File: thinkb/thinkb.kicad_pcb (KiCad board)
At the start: 2 copper layers, 2 parts, among them SW1 SW_Push

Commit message: Working on the PCB
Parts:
- added D10: 1N4148, footprints:diode_TH_SMD, F.Cu at (217.2, 48.7)
- added D11: 1N4148, footprints:diode_TH_SMD, F.Cu at (235.8, 48.9)
- added D12: 1N4148, footprints:diode_TH_SMD, F.Cu at (253.9, 49.6)
- added D13: 1N4148, footprints:diode_TH_SMD, F.Cu at (50.9, 65.8)
- added D14: 1N4148, footprints:diode_TH_SMD, F.Cu at (69.5, 65.7)
- added D15: 1N4148, footprints:diode_TH_SMD, F.Cu at (88.3, 66.0)
- added D16: 1N4148, footprints:diode_TH_SMD, F.Cu at (106.3, 66.1)
- added D17: 1N4148, footprints:diode_TH_SMD, F.Cu at (125.3, 67.1)
- added D18: 1N4148, footprints:diode_TH_SMD, F.Cu at (142.9, 66.8)
- added D19: 1N4148, footprints:diode_TH_SMD, F.Cu at (162.5, 66.8)
- added D2: 1N4148, footprints:diode_TH_SMD, F.Cu at (69.5, 48.2)
- added D20: 1N4148, footprints:diode_TH_SMD, F.Cu at (179.5, 66.0)
- added D21: 1N4148, footprints:diode_TH_SMD, F.Cu at (197.6, 66.0)
- added D22: 1N4148, footprints:diode_TH_SMD, F.Cu at (216.5, 65.8)
- added D23: 1N4148, footprints:diode_TH_SMD, F.Cu at (235.2, 66.1)
- added D24: 1N4148, footprints:diode_TH_SMD, F.Cu at (253.0, 65.8)
- added D25: 1N4148, footprints:diode_TH_SMD, F.Cu at (51.4, 83.1)
- added D26: 1N4148, footprints:diode_TH_SMD, F.Cu at (69.9, 82.4)
- added D27: 1N4148, footprints:diode_TH_SMD, F.Cu at (87.3, 82.7)
- added D28: 1N4148, footprints:diode_TH_SMD, F.Cu at (106.3, 82.8)
- added D29: 1N4148, footprints:diode_TH_SMD, F.Cu at (125.4, 83.0)
- added D3: 1N4148, footprints:diode_TH_SMD, F.Cu at (87.5, 47.9)
- added D30: 1N4148, footprints:diode_TH_SMD, F.Cu at (144.0, 82.8)
- added D31: 1N4148, footprints:diode_TH_SMD, F.Cu at (162.0, 82.9)
- added D32: 1N4148, footprints:diode_TH_SMD, F.Cu at (180.3, 83.1)
- added D33: 1N4148, footprints:diode_TH_SMD, F.Cu at (198.2, 83.4)
- added D34: 1N4148, footprints:diode_TH_SMD, F.Cu at (217.2, 83.0)
- added D35: 1N4148, footprints:diode_TH_SMD, F.Cu at (235.2, 82.8)
- added D36: 1N4148, footprints:diode_TH_SMD, F.Cu at (253.0, 82.9)
- added D37: 1N4148, footprints:diode_TH_SMD, F.Cu at (51.3, 100.7)
- added D38: 1N4148, footprints:diode_TH_SMD, F.Cu at (71.1, 98.1)
- added D39: 1N4148, footprints:diode_TH_SMD, F.Cu at (89.5, 99.1)
- added D4: 1N4148, footprints:diode_TH_SMD, F.Cu at (105.7, 48.9)
- added D40: 1N4148, footprints:diode_TH_SMD, F.Cu at (106.4, 99.7)
- added D41: 1N4148, footprints:diode_TH_SMD, F.Cu at (125.6, 100.1)
- added D42: 1N4148, footprints:diode_TH_SMD, F.Cu at (143.7, 100.2)
- added D43: 1N4148, footprints:diode_TH_SMD, F.Cu at (162.6, 99.4)
- added D44: 1N4148, footprints:diode_TH_SMD, F.Cu at (180.5, 99.5)
- added D45: 1N4148, footprints:diode_TH_SMD, F.Cu at (198.6, 100.3)
- added D46: 1N4148, footprints:diode_TH_SMD, F.Cu at (216.8, 99.9)
- added D47: 1N4148, footprints:diode_TH_SMD, F.Cu at (234.9, 99.9)
- added D48: 1N4148, footprints:diode_TH_SMD, F.Cu at (253.6, 100.5)
- added D49: 1N4148, footprints:diode_TH_SMD, F.Cu at (51.3, 116.4)
- added D5: 1N4148, footprints:diode_TH_SMD, F.Cu at (124.5, 49.9)
- added D50: 1N4148, footprints:diode_TH_SMD, F.Cu at (69.9, 116.3)
- added D51: 1N4148, footprints:diode_TH_SMD, F.Cu at (88.9, 115.9)
- added D52: 1N4148, footprints:diode_TH_SMD, F.Cu at (107.8, 116.8)
- added D53: 1N4148, footprints:diode_TH_SMD, F.Cu at (126.4, 117.2)
- added D54: 1N4148, footprints:diode_TH_SMD, F.Cu at (144.1, 116.3)
- added D55: 1N4148, footprints:diode_TH_SMD, F.Cu at (161.7, 116.6)
- added D56: 1N4148, footprints:diode_TH_SMD, F.Cu at (180.5, 116.0)
- added D57: 1N4148, footprints:diode_TH_SMD, F.Cu at (198.7, 116.4)
- added D58: 1N4148, footprints:diode_TH_SMD, F.Cu at (216.5, 116.8)
- added D59: 1N4148, footprints:diode_TH_SMD, F.Cu at (234.1, 116.8)
- added D6: 1N4148, footprints:diode_TH_SMD, F.Cu at (143.8, 49.1)
- added D60: 1N4148, footprints:diode_TH_SMD, F.Cu at (253.3, 116.9)
- added D7: 1N4148, footprints:diode_TH_SMD, F.Cu at (162.6, 49.0)
- added D8: 1N4148, footprints:diode_TH_SMD, F.Cu at (180.2, 48.5)
- added D9: 1N4148, footprints:diode_TH_SMD, F.Cu at (198.6, 48.4)
- added SW10: SW_Push, footprints:Choc_PG1350_Choc_Spacing, F.Cu at (215.6, 45.2)
- added SW11: SW_Push, footprints:Choc_PG1350_Choc_Spacing, F.Cu at (234.0, 45.6)
- added SW12: SW_Push, footprints:Choc_PG1350_Choc_Spacing, F.Cu at (252.0, 45.9)
- added SW13: SW_Push, footprints:Choc_PG1350_Choc_Spacing, F.Cu at (49.4, 62.4)
- added SW14: SW_Push, footprints:Choc_PG1350_Choc_Spacing, F.Cu at (67.9, 62.3)
- added SW15: SW_Push, footprints:Choc_PG1350_Choc_Spacing, F.Cu at (86.3, 62.4)
- added SW16: SW_Push, footprints:Choc_PG1350_Choc_Spacing, F.Cu at (104.3, 62.6)
- added SW17: SW_Push, footprints:Choc_PG1350_Choc_Spacing, F.Cu at (123.0, 63.1)
- added SW18: SW_Push, footprints:Choc_PG1350_Choc_Spacing, F.Cu at (141.5, 63.2)
- added SW19: SW_Push, footprints:Choc_PG1350_Choc_Spacing, F.Cu at (160.2, 63.2)
- added SW2: SW_Push, footprints:Choc_PG1350_Choc_Spacing, F.Cu at (67.4, 44.8)
- added SW20: SW_Push, footprints:Choc_PG1350_Choc_Spacing, F.Cu at (178.3, 62.5)
- added SW21: SW_Push, footprints:Choc_PG1350_Choc_Spacing, F.Cu at (196.5, 62.5)
- added SW22: SW_Push, footprints:Choc_PG1350_Choc_Spacing, F.Cu at (214.9, 62.4)
- added SW23: SW_Push, footprints:Choc_PG1350_Choc_Spacing, F.Cu at (233.4, 62.5)
- added SW24: SW_Push, footprints:Choc_PG1350_Choc_Spacing, F.Cu at (251.6, 62.6)
- added SW25: SW_Push, footprints:Choc_PG1350_Choc_Spacing, F.Cu at (49.2, 79.5)
- added SW26: SW_Push, footprints:Choc_PG1350_Choc_Spacing, F.Cu at (67.8, 79.1)
- added SW27: SW_Push, footprints:Choc_PG1350_Choc_Spacing, F.Cu at (86.3, 79.2)
- added SW28: SW_Push, footprints:Choc_PG1350_Choc_Spacing, F.Cu at (104.4, 79.1)
- added SW29: SW_Push, footprints:Choc_PG1350_Choc_Spacing, F.Cu at (123.7, 79.3)
- added SW3: SW_Push, footprints:Choc_PG1350_Choc_Spacing, F.Cu at (85.6, 44.4)
- added SW30: SW_Push, footprints:Choc_PG1350_Choc_Spacing, F.Cu at (142.1, 79.3)
- added SW31: SW_Push, footprints:Choc_PG1350_Choc_Spacing, F.Cu at (160.3, 79.6)
- added SW32: SW_Push, footprints:Choc_PG1350_Choc_Spacing, F.Cu at (178.4, 79.5)
- added SW33: SW_Push, footprints:Choc_PG1350_Choc_Spacing, F.Cu at (196.5, 79.9)
- added SW34: SW_Push, footprints:Choc_PG1350_Choc_Spacing, F.Cu at (214.7, 79.5)
- added SW35: SW_Push, footprints:Choc_PG1350_Choc_Spacing, F.Cu at (233.1, 79.4)
- added SW36: SW_Push, footprints:Choc_PG1350_Choc_Spacing, F.Cu at (251.9, 79.7)
- added SW37: SW_Push, footprints:Choc_PG1350_Choc_Spacing, F.Cu at (49.5, 96.9)
- added SW38: SW_Push, footprints:Choc_PG1350_Choc_Spacing, F.Cu at (69.4, 94.8)
- added SW39: SW_Push, footprints:Choc_PG1350_Choc_Spacing, F.Cu at (87.7, 95.7)
- added SW4: SW_Push, footprints:Choc_PG1350_Choc_Spacing, F.Cu at (104.1, 45.4)
- added SW40: SW_Push, footprints:Choc_PG1350_Choc_Spacing, F.Cu at (104.7, 96.1)
- added SW41: SW_Push, footprints:Choc_PG1350_Choc_Spacing, F.Cu at (123.7, 96.7)
- added SW42: SW_Push, footprints:Choc_PG1350_Choc_Spacing, F.Cu at (141.9, 96.5)
- added SW43: SW_Push, footprints:Choc_PG1350_Choc_Spacing, F.Cu at (160.4, 96.2)
- added SW44: SW_Push, footprints:Choc_PG1350_Choc_Spacing, F.Cu at (178.8, 96.2)
- added SW45: SW_Push, footprints:Choc_PG1350_Choc_Spacing, F.Cu at (196.5, 96.8)
- added SW46: SW_Push, footprints:Choc_PG1350_Choc_Spacing, F.Cu at (214.7, 96.5)
- added SW47: SW_Push, footprints:Choc_PG1350_Choc_Spacing, F.Cu at (232.9, 96.2)
- added SW48: SW_Push, footprints:Choc_PG1350_Choc_Spacing, F.Cu at (251.4, 97.0)
- added SW49: SW_Push, footprints:Choc_PG1350_Choc_Spacing, F.Cu at (49.3, 112.9)
- added SW5: SW_Push, footprints:Choc_PG1350_Choc_Spacing, F.Cu at (122.7, 46.3)
- added SW50: SW_Push, footprints:Choc_PG1350_Choc_Spacing, F.Cu at (68.4, 112.9)
- added SW51: SW_Push, footprints:Choc_PG1350_Choc_Spacing, F.Cu at (87.1, 112.7)
- added SW52: SW_Push, footprints:Choc_PG1350_Choc_Spacing, F.Cu at (106.6, 113.3)
- added SW53: SW_Push, footprints:Choc_PG1350_Choc_Spacing, F.Cu at (124.5, 113.3)
- added SW54: SW_Push, footprints:Choc_PG1350_Choc_Spacing, F.Cu at (142.1, 113.0)
- added SW55: SW_Push, footprints:Choc_PG1350_Choc_Spacing, F.Cu at (160.2, 113.1)
- added SW56: SW_Push, footprints:Choc_PG1350_Choc_Spacing, F.Cu at (178.7, 112.6)
- added SW57: SW_Push, footprints:Choc_PG1350_Choc_Spacing, F.Cu at (196.8, 113.0)
- added SW58: SW_Push, footprints:Choc_PG1350_Choc_Spacing, F.Cu at (215.0, 113.2)
- added SW59: SW_Push, footprints:Choc_PG1350_Choc_Spacing, F.Cu at (232.4, 113.3)
- added SW6: SW_Push, footprints:Choc_PG1350_Choc_Spacing, F.Cu at (141.4, 45.5)
- added SW60: SW_Push, footprints:Choc_PG1350_Choc_Spacing, F.Cu at (251.3, 113.2)
- added SW7: SW_Push, footprints:Choc_PG1350_Choc_Spacing, F.Cu at (160.6, 45.5)
- added SW8: SW_Push, footprints:Choc_PG1350_Choc_Spacing, F.Cu at (178.4, 45.2)
- added SW9: SW_Push, footprints:Choc_PG1350_Choc_Spacing, F.Cu at (196.7, 45.0)
- D1: footprint Diode_THT:D_DO-35_SOD27_P7.62mm_Horizontal -> footprints:diode_TH_SMD
- moved SW1 101.3 mm to (49.4, 44.8)
- moved D1 94.0 mm to (51.1, 48.3), turned to 0 degrees

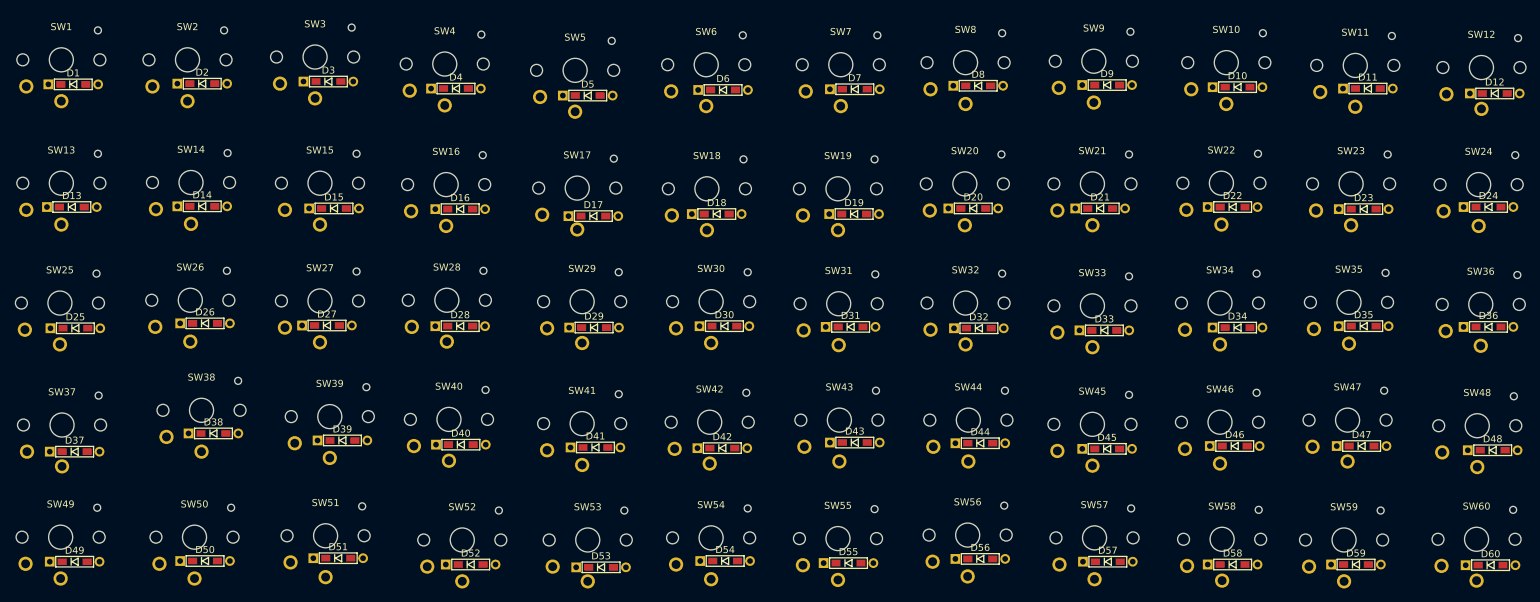
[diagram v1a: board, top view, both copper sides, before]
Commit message: Aligned all the switches
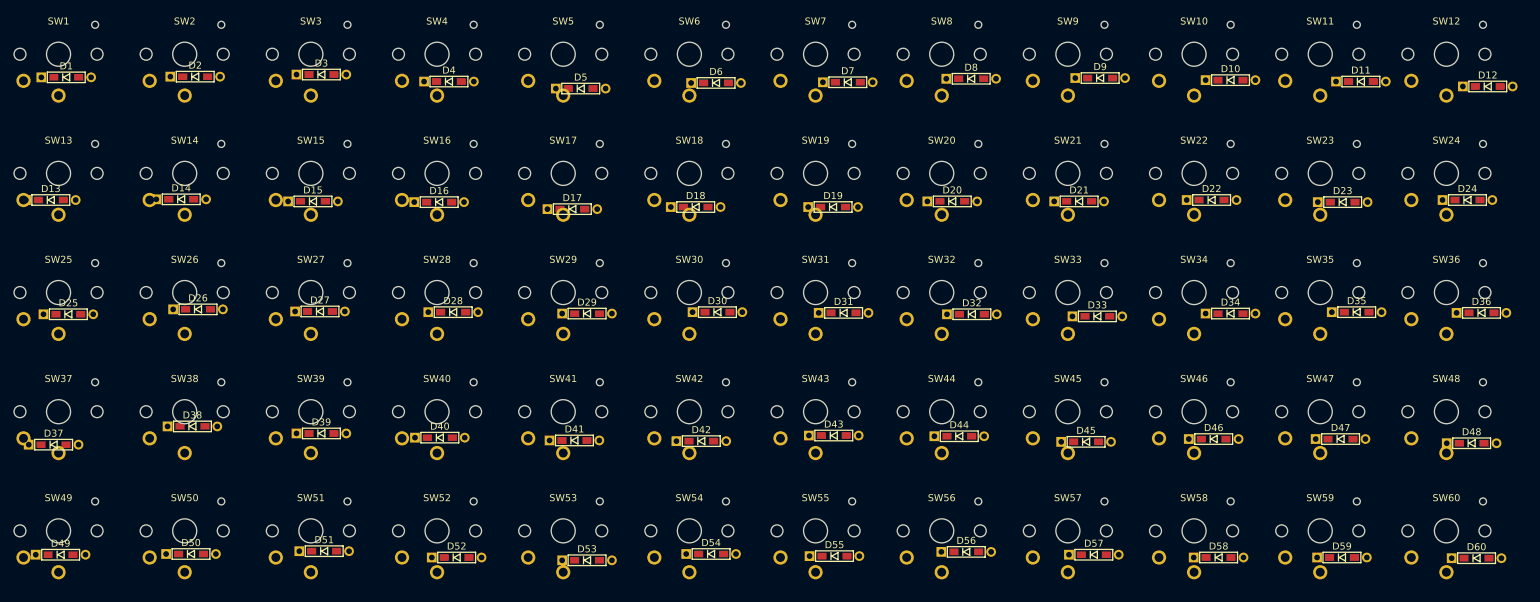
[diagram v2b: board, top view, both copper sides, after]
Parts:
- moved SW12 5.35 mm to (247.0, 44.0)
- moved SW11 5.25 mm to (229.0, 44.0)
- moved SW36 5.19 mm to (247.0, 78.0)
- moved SW24 4.87 mm to (247.0, 61.0)
- moved SW48 4.83 mm to (247.0, 95.0)
- moved SW10 4.75 mm to (211.0, 44.0)
- moved SW23 4.65 mm to (229.0, 61.0)
- moved SW60 4.46 mm to (247.0, 112.0)
- moved SW35 4.33 mm to (229.0, 78.0)
- moved SW58 4.18 mm to (211.0, 112.0)
- moved SW22 4.14 mm to (211.0, 61.0)
- moved SW47 4.08 mm to (229.0, 95.0)
- moved SW34 3.99 mm to (211.0, 78.0)
- moved SW46 3.99 mm to (211.0, 95.0)
- moved SW44 3.98 mm to (175.0, 95.0)
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
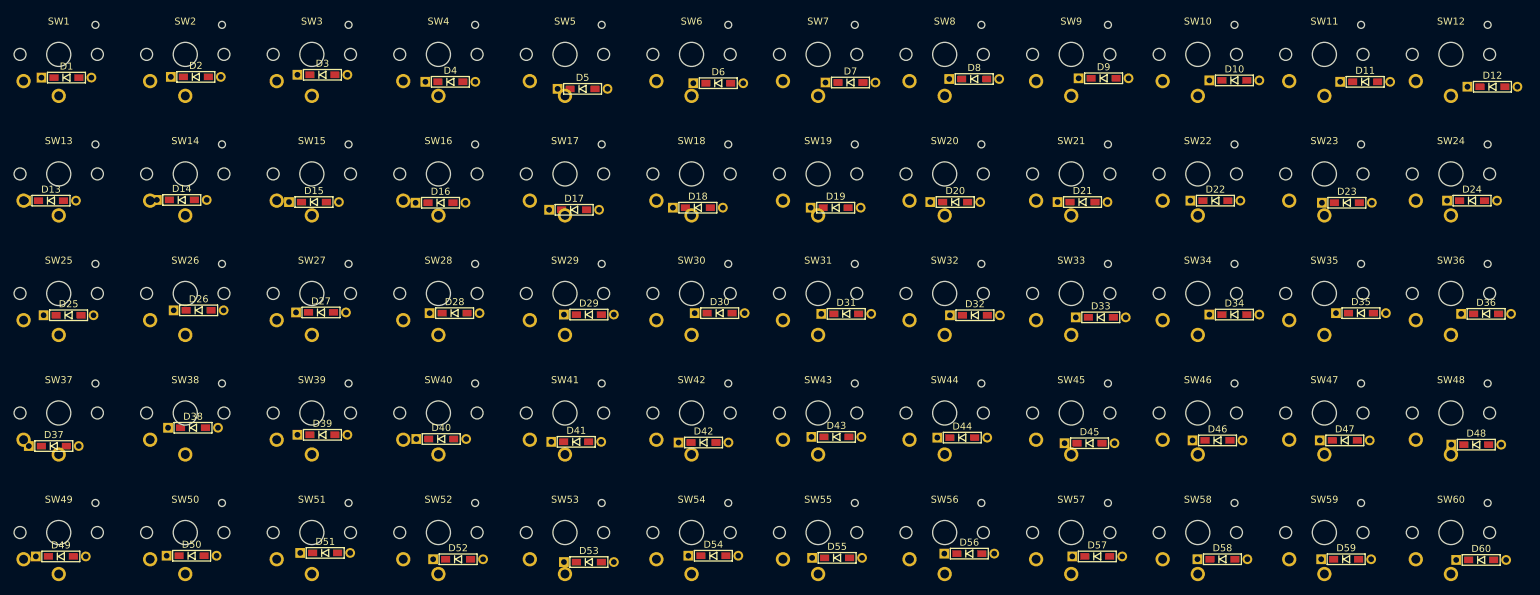
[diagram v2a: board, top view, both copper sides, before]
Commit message: Aligned diodes
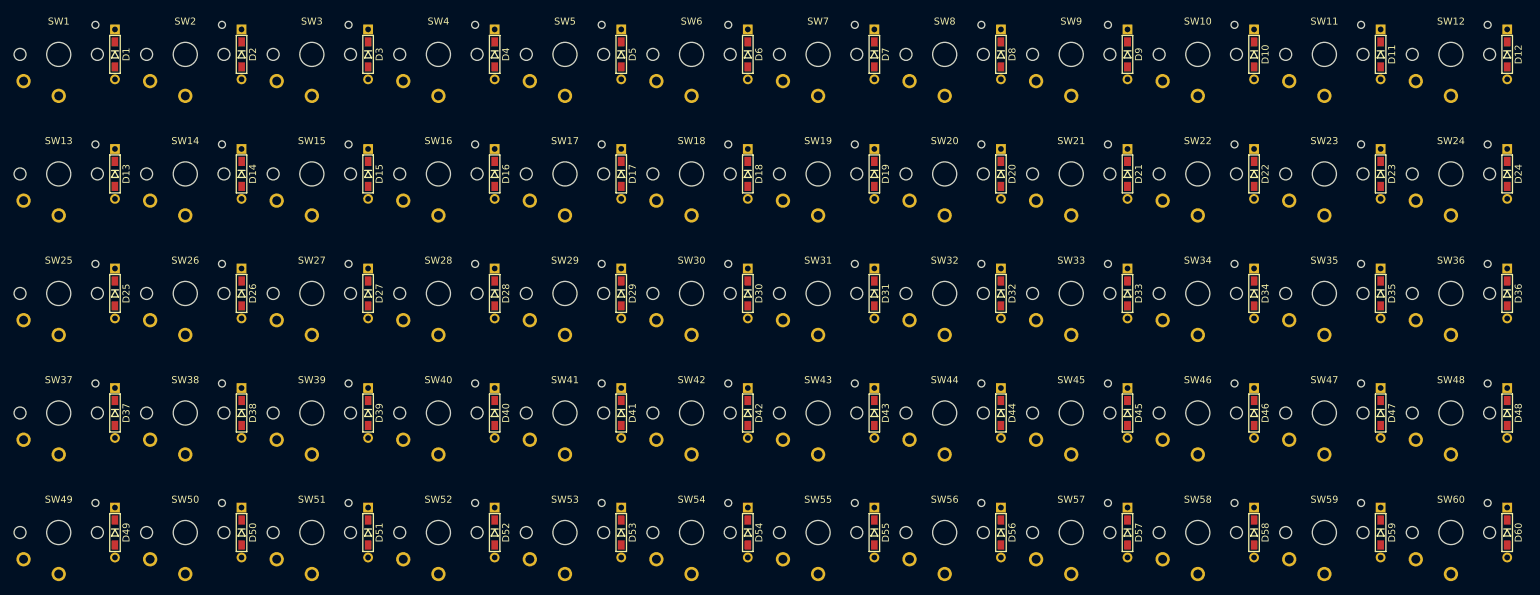
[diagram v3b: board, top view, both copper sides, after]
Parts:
- moved D37 9.89 mm to (57.0, 95.0), turned to 270 degrees
- moved D13 9.86 mm to (57.0, 61.0), turned to 270 degrees
- moved D14 9.27 mm to (75.0, 61.0), turned to 270 degrees
- moved D16 8.72 mm to (111.0, 61.0), turned to 270 degrees
- moved D15 8.68 mm to (93.0, 61.0), turned to 270 degrees
- moved D18 8.57 mm to (147.0, 61.0), turned to 270 degrees
- moved D40 8.45 mm to (111.0, 95.0), turned to 270 degrees
- moved D17 8.42 mm to (129.0, 61.0), turned to 270 degrees
- moved D49 8.42 mm to (57.0, 112.0), turned to 270 degrees
- moved D50 7.83 mm to (75.0, 112.0), turned to 270 degrees
- moved D1 7.65 mm to (57.0, 44.0), turned to 270 degrees
- moved D20 7.63 mm to (183.0, 61.0), turned to 270 degrees
- moved D41 7.60 mm to (129.0, 95.0), turned to 270 degrees
- moved D42 7.57 mm to (147.0, 95.0), turned to 270 degrees
- moved D21 7.55 mm to (201.0, 61.0), turned to 270 degrees
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
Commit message: Ready to shape the thumb cluster
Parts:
- moved D10 64.0 mm to (283.0, 44.0)
- moved D11 64.0 mm to (301.0, 44.0)
- moved D12 64.0 mm to (319.0, 44.0)
- moved D19 64.0 mm to (229.0, 61.0)
- moved D20 64.0 mm to (247.0, 61.0)
- moved D21 64.0 mm to (265.0, 61.0)
- moved D22 64.0 mm to (283.0, 61.0)
- moved D23 64.0 mm to (301.0, 61.0)
- moved D24 64.0 mm to (319.0, 61.0)
- moved D31 64.0 mm to (229.0, 78.0)
- moved D32 64.0 mm to (247.0, 78.0)
- moved D33 64.0 mm to (265.0, 78.0)
- moved D34 64.0 mm to (283.0, 78.0)
- moved D35 64.0 mm to (301.0, 78.0)
- moved D36 64.0 mm to (319.0, 78.0)
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
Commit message: WIP on thumb cluster
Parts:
- moved D52 25.5 mm to (148.0, 137.4), turned to 229.5 degrees
- moved SW52 20.3 mm to (141.9, 132.3), turned to 319.5 degrees
- moved SW57 20.3 mm to (193.1, 132.3), turned to 40.5 degrees
- moved D57 15.3 mm to (199.2, 127.1), turned to 310.5 degrees
- moved D51 12.9 mm to (132.5, 124.8), turned to 243 degrees
- moved SW51 9.52 mm to (125.4, 121.2), turned to 333 degrees
- moved SW58 9.52 mm to (209.6, 121.2), turned to 27 degrees
- moved D58 6.46 mm to (216.7, 117.6), turned to 297 degrees
- moved D50 4.47 mm to (114.5, 116.2), turned to 256.5 degrees
- moved SW50 2.91 mm to (106.7, 114.3), turned to 346.5 degrees
- moved SW59 2.91 mm to (228.3, 114.3), turned to 13.5 degrees
- moved D59 2.01 mm to (236.0, 112.5), turned to 283.5 degrees

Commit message: Shaped the vertical stagger
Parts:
- moved D54 45.8 mm to (175.0, 137.5)
- moved SW54 45.8 mm to (167.0, 137.5)
- moved D55 31.2 mm to (175.0, 120.5)
- moved SW55 31.2 mm to (167.0, 120.5)
- moved D53 15.0 mm to (140.2, 110.0), turned to 243 degrees
- moved SW56 11.4 mm to (201.9, 106.4), turned to 27 degrees
- moved SW53 11.4 mm to (133.1, 106.4), turned to 333 degrees
- moved D56 8.00 mm to (209.0, 102.8), turned to 297 degrees
- moved D1 4.50 mm to (32.0, 48.5)
- moved D11 4.50 mm to (301.0, 48.5)
- moved D12 4.50 mm to (319.0, 48.5)
- moved D13 4.50 mm to (32.0, 65.5)
- moved D14 4.50 mm to (50.0, 65.5)
- moved D2 4.50 mm to (50.0, 48.5)
- moved D23 4.50 mm to (301.0, 65.5)
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
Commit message: Shaped the keyboard in general
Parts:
- moved D12 33.0 mm to (294.3, 26.7), turned to 282.5 degrees
- moved SW12 31.7 mm to (286.5, 28.4), turned to 12.5 degrees
- moved D24 30.6 mm to (298.0, 43.3), turned to 282.5 degrees
- moved D11 30.2 mm to (276.7, 30.6), turned to 282.5 degrees
- moved SW24 29.2 mm to (290.2, 45.0), turned to 12.5 degrees
- moved SW11 29.0 mm to (268.9, 32.3), turned to 12.5 degrees
- moved D36 28.5 mm to (301.7, 59.9), turned to 282.5 degrees
- moved D10 28.4 mm to (258.2, 30.1), turned to 282.5 degrees
- moved D23 27.6 mm to (280.4, 47.2), turned to 282.5 degrees
- moved SW10 27.5 mm to (250.4, 31.8), turned to 12.5 degrees
- moved SW36 27.0 mm to (293.9, 61.6), turned to 12.5 degrees
- moved D9 26.8 mm to (240.1, 31.5), turned to 282.5 degrees
- moved D48 26.8 mm to (305.4, 76.5), turned to 282.5 degrees
- moved SW1 26.4 mm to (41.1, 28.4), turned to 347.5 degrees
- moved SW23 26.3 mm to (272.6, 48.9), turned to 12.5 degrees
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
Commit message: Fine-aligned upper thumb buttons
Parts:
- moved SW1 115.3 mm to (25.4, 142.6), turned to 27 degrees
- moved SW13 112.9 mm to (33.1, 157.8), turned to 27 degrees
- moved SW25 111.5 mm to (40.8, 172.9), turned to 27 degrees
- moved SW37 111.4 mm to (48.5, 188.1), turned to 27 degrees
- moved D1 110.1 mm to (32.5, 139.0), turned to 297 degrees
- moved D13 107.5 mm to (40.2, 154.1), turned to 297 degrees
- moved D25 106.2 mm to (48.0, 169.3), turned to 297 degrees
- moved D37 106.0 mm to (55.7, 184.4), turned to 297 degrees
- moved SW2 103.6 mm to (41.4, 134.4), turned to 27 degrees
- moved SW14 100.9 mm to (49.1, 149.6), turned to 27 degrees
- moved SW26 99.4 mm to (56.9, 164.7), turned to 27 degrees
- moved SW38 99.3 mm to (64.6, 179.9), turned to 27 degrees
- moved D2 98.4 mm to (48.6, 130.8), turned to 297 degrees
- moved D14 95.6 mm to (56.3, 146.0), turned to 297 degrees
- moved D26 94.0 mm to (64.0, 161.1), turned to 297 degrees
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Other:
- board outline added: 36.6 x 30.1 mm
